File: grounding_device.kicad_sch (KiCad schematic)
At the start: 118 parts, among them IC1 NE555P, IC2 NE555P, IC3 NE555P, IC4 NE555P, Q1 2N2222, Q10 2N2222, Q11 2N2222, Q12 2N2222, Q2 2N2222, Q3 2N2222, Q4 2N2222, Q5 2N2222, Q6 2N2222, Q7 2N2222, Q8 2N2222, Q9 2N2222

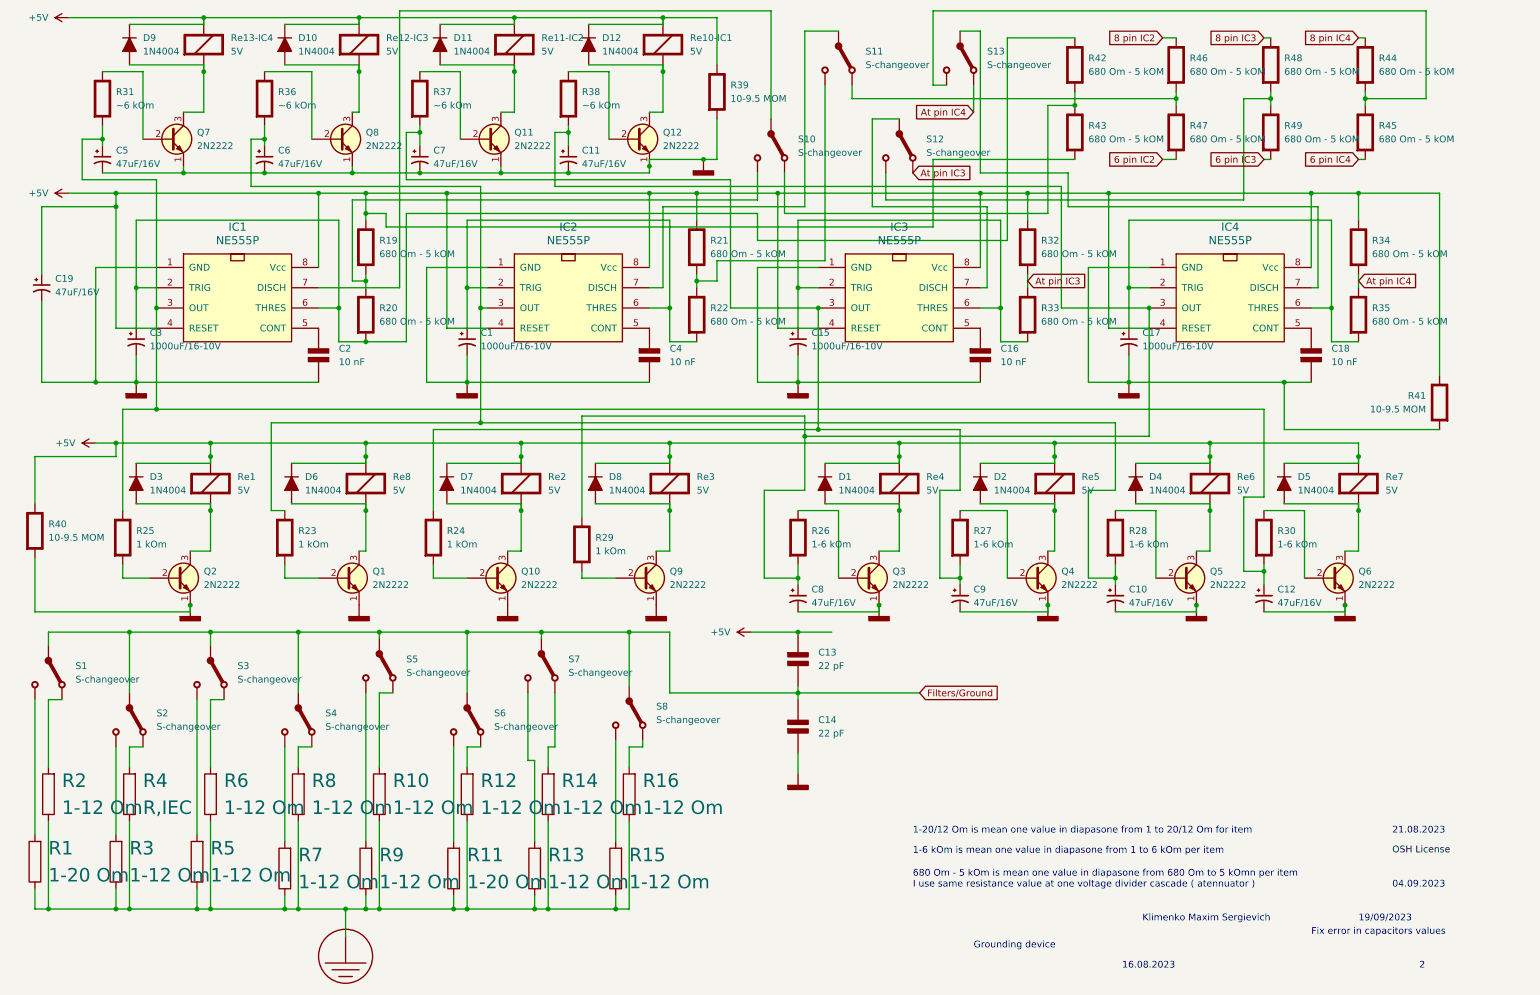
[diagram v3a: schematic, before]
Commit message: Upgrade to 4 revision
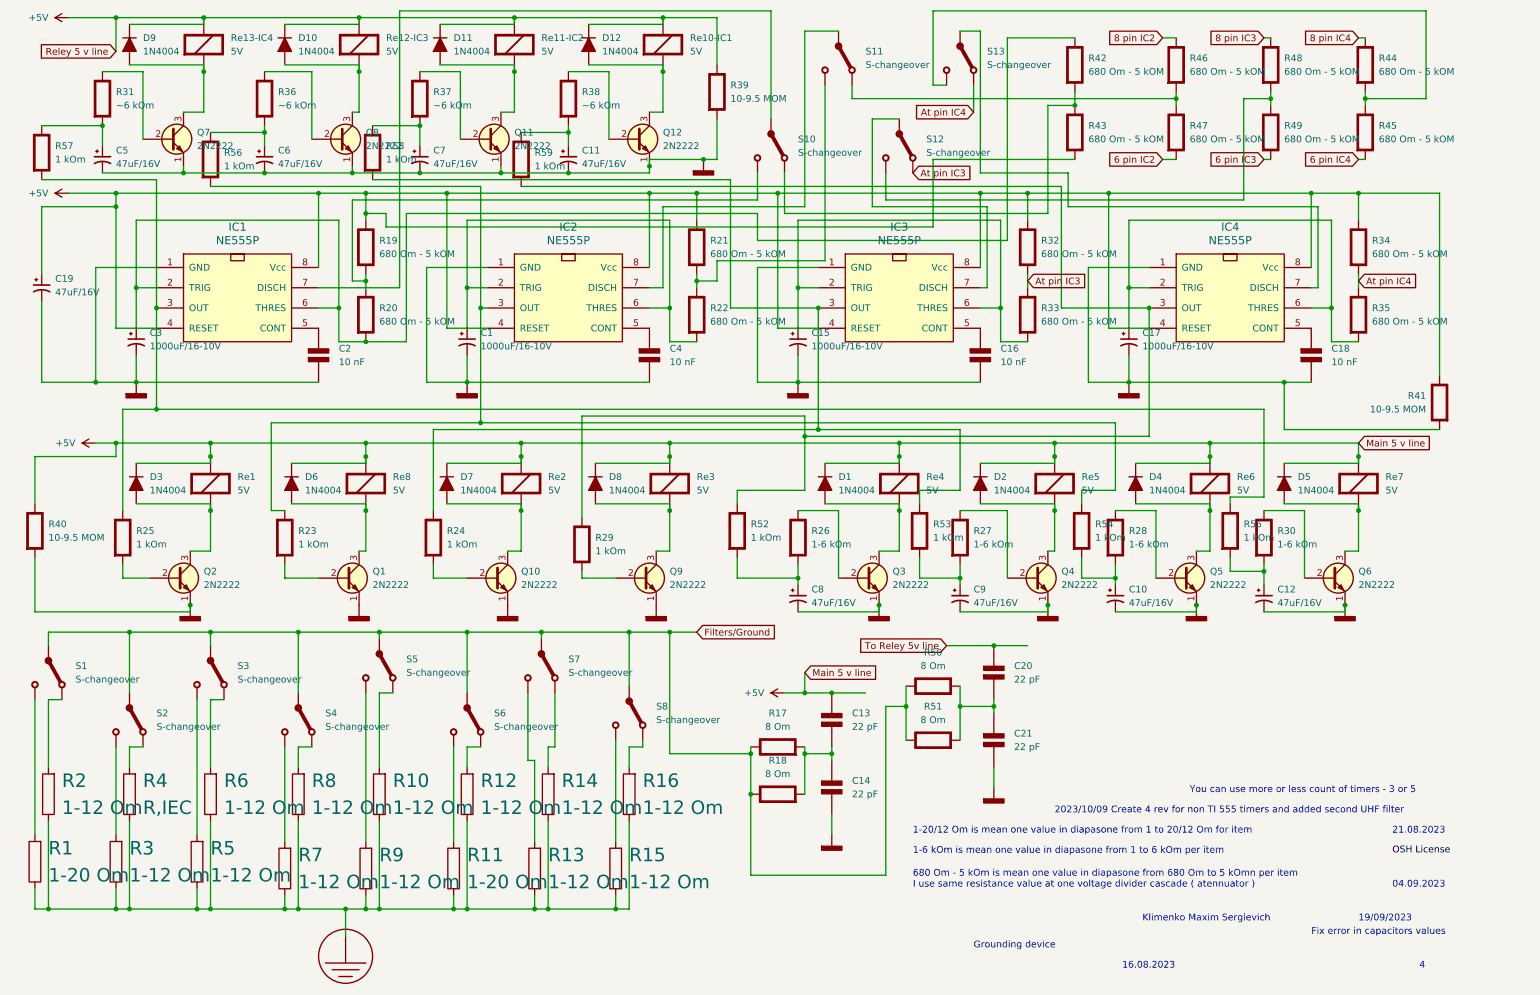
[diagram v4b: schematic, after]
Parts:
- added C20, C21: 22 pF, symbol PCM_Elektuur:C
- added R17, R18, R50, R51: 8 Om, symbol PCM_Elektuur:R
- added R52, R53, R54, R55, R56, R57, R58, R59: 1 kOm, symbol PCM_Elektuur:R
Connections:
- net 0: now also C21.2 (-)
- net Filters/Ground: now also R17.1 (+), R18.1 (+), R50.1 (+), R51.1 (+); no longer C13.2 (-), C14.1 (+)
- new net: C20.2 (-), C21.1 (+), R50.2 (-), R51.2 (-)
- new net: IC1.3 (OUT), R25.1 (+), R55.1 (+), R57.2 (-)
- new net: C5.1, R31.2 (-), R57.1 (+)
- new net: C12.1, R30.2 (-), R55.2 (-)
- new net: C11.1, R38.2 (-), R59.1 (+)
- new net: C7.1, R37.2 (-), R58.1 (+)
- new net: C9.1, R27.2 (-), R53.2 (-)
- new net: IC4.3 (OUT), R29.1 (+), R52.1 (+), R59.2 (-)
- new net: C8.1, R26.2 (-), R52.2 (-)
- new net: C13.2 (-), C14.1 (+), R17.2 (-), R18.2 (-)
- new net: IC3.3 (OUT), R24.1 (+), R53.1 (+), R58.2 (-)
- new net: C6.1, R36.2 (-), R56.1 (+)
- new net: IC2.3 (OUT), R23.1 (+), R54.1 (+), R56.2 (-)
- new net: C10.1, R28.2 (-), R54.2 (-)
- new net To Reley 5v line : C20.1 (+)
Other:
- note added: "2023/10/09 Create 4 rev for non TI 555 timers and added second UHF filter"
- note added: "4"
- note added: "You can use more or less count of timers - 3 or 5"
- note removed: "2"
- moved on the sheet: C13, C14

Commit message: Upgrade
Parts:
- added C22: 47uF or 100uF, symbol PCM_Elektuur:C
- added C23: 680pF, symbol PCM_Elektuur:C
- added R60, R61, R62, R63: 8 Om, symbol PCM_Elektuur:R
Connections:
- net Filters/Ground: now also R60.1 (+), R61.1 (+), R62.1 (+), R63.1 (+)
- net To Reley 5v line : now also C22.1 (+), C23.1 (+)
- new net: C22.2 (-), R60.2 (-), R61.2 (-)
- new net: C23.2 (-), R62.2 (-), R63.2 (-)
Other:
- note added: "Resistor array must be created for first"
- note added: "This 2 filters must be soldering after resistors array to (+)line before place rele"
- note added: "Updated 2023.10.23"

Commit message: Upgrade
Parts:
- removed R51, R60, R63: 8 Om, symbol PCM_Elektuur:R
- added C24: 47uF or 10uF, symbol PCM_Elektuur:C
- C22: value 47uF or 100uF -> 47uF or 10uF
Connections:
- net Filters/Ground: now also C24.1 (+); no longer R18.1 (+)
- net To Reley 5v line : now also R18.1 (+)
- net at C13.2 (-), C14.1 (+), R17.2 (-): no longer R18.2 (-)
- new net: C24.2 (-), R18.2 (-)
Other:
- note added: "04.03.2024"
- moved on the sheet: R17, R50, R61, R62

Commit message: Upgrade
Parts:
- C22, C24: value 47uF or 10uF -> 1uF
- C23: value 680pF -> 100pF
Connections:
- net 0: now also C24.1 (+)
- net Filters/Ground: now also R18.1 (+); no longer C24.1 (+)
- net To Reley 5v line : no longer R18.1 (+)
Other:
- moved on the sheet: C24, R18
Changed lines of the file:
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@@
 (kicad_sch (version 20230121) (generator eeschema)
   (paper "A4")
+  (junction (at 165.1 167.64) (diameter 0) (color 0 0 0 0)
+  )
   (junction (at 26.67 83.82) (diameter 0) (color 0 0 0 0)
   )
@@
   (junction (at 106.68 97.79) (diameter 0) (color 0 0 0 0)
   )
-  (junction (at 240.03 133.35) (diameter 0) (color 0 0 0 0)
-  )
   (junction (at 73.66 182.88) (diameter 0) (color 0 0 0 0)
   )
@@
   (junction (at 201.93 48.26) (diameter 0) (color 0 0 0 0)
   )
-  (junction (at 240.03 154.94) (diameter 0) (color 0 0 0 0)
-  )
   (junction (at 247.65 30.48) (diameter 0) (color 0 0 0 0)
   )
@@
   (junction (at 162.56 92.71) (diameter 0) (color 0 0 0 0)
   )
+  (junction (at 170.18 176.53) (diameter 0) (color 0 0 0 0)
+  )
   (junction (at 160.02 93.98) (diameter 0) (color 0 0 0 0)
   )
@@
     (stroke (width 0) (type default))
   )
+  (wire (pts (xy 156.21 187.96) (xy 170.18 187.96))
+    (stroke (width 0) (type default))
+  )
   (wire (pts (xy 48.26 182.88) (xy 62.23 182.88))
     (stroke (width 0) (type default))
@@
     (stroke (width 0) (type default))
   )
-  (wire (pts (xy 165.1 165.1) (xy 165.1 168.91))
+  (wire (pts (xy 165.1 165.1) (xy 165.1 167.64))
     (stroke (width 0) (type default))
   )
@@
     (stroke (width 0) (type default))
   )
-  (wire (pts (xy 224.79 69.85) (xy 208.28 69.85))
+  (wire (pts (xy 156.21 167.64) (xy 165.1 167.64))
     (stroke (width 0) (type default))
   )
-  (wire (pts (xy 173.99 115.57) (xy 177.8 115.57))
+  (wire (pts (xy 224.79 69.85) (xy 208.28 69.85))
     (stroke (width 0) (type default))
   )
-  (wire (pts (xy 256.54 154.94) (xy 251.46 154.94))
+  (wire (pts (xy 173.99 115.57) (xy 177.8 115.57))
     (stroke (width 0) (type default))
   )
@@
     (stroke (width 0) (type default))
   )
-  (wire (pts (xy 240.03 154.94) (xy 240.03 153.67))
+  (wire (pts (xy 240.03 153.67) (xy 240.03 157.48))
     (stroke (width 0) (type default))
   )
@@
     (stroke (width 0) (type default))
   )
-  (wire (pts (xy 240.03 157.48) (xy 240.03 154.94))
-    (stroke (width 0) (type default))
-  )
   (wire (pts (xy 213.36 160.02) (xy 199.39 160.02))
     (stroke (width 0) (type default))
@@
     (stroke (width 0) (type default))
   )
-  (wire (pts (xy 240.03 133.35) (xy 251.46 133.35))
-    (stroke (width 0) (type default))
-  )
   (wire (pts (xy 154.94 73.66) (xy 162.56 73.66))
     (stroke (width 0) (type default))
@@
     (stroke (width 0) (type default))
   )
-  (wire (pts (xy 248.92 134.62) (xy 248.92 154.94))
-    (stroke (width 0) (type default))
-  )
-  (wire (pts (xy 248.92 154.94) (xy 240.03 154.94))
-    (stroke (width 0) (type default))
-  )
   (wire (pts (xy 151.13 57.15) (xy 151.13 52.07))
     (stroke (width 0) (type default))
@@
     (stroke (width 0) (type default))
   )
-  (wire (pts (xy 256.54 134.62) (xy 248.92 134.62))
-    (stroke (width 0) (type default))
-  )
   (wire (pts (xy 99.06 69.85) (xy 99.06 46.99))
     (stroke (width 0) (type default))
@@
     (stroke (width 0) (type default))
   )
+  (wire (pts (xy 170.18 176.53) (xy 149.86 176.53))
+    (stroke (width 0) (type default))
+  )
   (wire (pts (xy 175.26 163.83) (xy 175.26 176.53))
     (stroke (width 0) (type default))
@@
     (stroke (width 0) (type default))
   )
-  (wire (pts (xy 251.46 154.94) (xy 251.46 133.35))
-    (stroke (width 0) (type default))
-  )
   (wire (pts (xy 74.93 49.53) (xy 74.93 64.77))
     (stroke (width 0) (type default))
@@
     (stroke (width 0) (type default))
   )
+  (wire (pts (xy 170.18 187.96) (xy 170.18 176.53))
+    (stroke (width 0) (type default))
+  )
   (wire (pts (xy 147.32 104.14) (xy 160.02 104.14))
     (stroke (width 0) (type default))
@@
     (stroke (width 0) (type default))
   )
+  (wire (pts (xy 165.1 167.64) (xy 165.1 168.91))
+    (stroke (width 0) (type default))
+  )
   (wire (pts (xy 130.81 48.26) (xy 139.7 48.26))
     (stroke (width 0) (type default))
@@
     (stroke (width 0) (type default))
   )
-  (wire (pts (xy 175.26 176.53) (xy 149.86 176.53))
+  (wire (pts (xy 175.26 176.53) (xy 170.18 176.53))
     (stroke (width 0) (type default))
   )
@@
     )
   )
-  (symbol (lib_id "PCM_Elektuur:C") (at 256.54 139.7 0) (unit 1)
+  (symbol (lib_id "PCM_Elektuur:C") (at 156.21 172.72 0) (unit 1)
     (in_bom yes) (on_board yes) (dnp no) (fields_autoplaced)
-    (property "Reference" "C24" (at 260.35 138.43 0)
+    (property "Reference" "C24" (at 160.02 171.45 0)
       (effects (font (size 1.27 1.27)) (justify left))
     )
-    (property "Value" "47uF or 10uF" (at 260.35 140.97 0)
+    (property "Value" "1uF" (at 160.02 173.99 0)
       (effects (font (size 1.27 1.27)) (justify left))
     )
-    (property "Footprint" "" (at 256.54 139.7 0)
+    (property "Footprint" "" (at 156.21 172.72 0)
       (effects (font (size 1.27 1.27)) hide)
     )
-    (property "Datasheet" "" (at 256.54 139.7 0)
+    (property "Datasheet" "" (at 156.21 172.72 0)
       (effects (font (size 1.27 1.27)) hide)
     )
-    (property "Indicator" "+" (at 255.27 136.525 0)
+    (property "Indicator" "+" (at 154.94 169.545 0)
       (effects (font (size 1.27 1.27)) hide)
     )
-    (property "Rating" "V" (at 255.905 142.875 0)
+    (property "Rating" "V" (at 155.575 175.895 0)
       (effects (font (size 1.27 1.27)) (justify right) hide)
     )
@@
       (effects (font (size 1.27 1.27)) (justify left))
     )
-    (property "Value" "47uF or 10uF" (at 217.17 139.7 0)
+    (property "Value" "1uF" (at 217.17 139.7 0)
       (effects (font (size 1.27 1.27)) (justify left))
     )
@@
     )
   )
-  (symbol (lib_id "PCM_Elektuur:R") (at 256.54 149.86 180) (unit 1)
+  (symbol (lib_id "PCM_Elektuur:R") (at 156.21 182.88 180) (unit 1)
     (in_bom yes) (on_board yes) (dnp no) (fields_autoplaced)
-    (property "Reference" "R18" (at 259.715 148.59 0)
+    (property "Reference" "R18" (at 159.385 181.61 0)
       (effects (font (size 1.27 1.27)) (justify right))
     )
-    (property "Value" "8 Om" (at 259.715 151.13 0)
+    (property "Value" "8 Om" (at 159.385 184.15 0)
       (effects (font (size 1.27 1.27)) (justify right))
     )
-    (property "Footprint" "" (at 256.54 149.86 0)
+    (property "Footprint" "" (at 156.21 182.88 0)
       (effects (font (size 1.27 1.27)) hide)
     )
-    (property "Datasheet" "" (at 256.54 149.86 0)
+    (property "Datasheet" "" (at 156.21 182.88 0)
       (effects (font (size 1.27 1.27)) hide)
     )
-    (property "Indicator" "+" (at 259.715 153.035 0)
+    (property "Indicator" "+" (at 159.385 186.055 0)
       (effects (font (size 1.27 1.27)) hide)
     )
-    (property "Rating" "W" (at 254 146.685 0)
+    (property "Rating" "W" (at 153.67 179.705 0)
       (effects (font (size 1.27 1.27)) (justify left) hide)
     )
@@
       (effects (font (size 1.27 1.27)) (justify left))
     )
-    (property "Value" "680pF" (at 243.84 139.7 0)
+    (property "Value" "100pF" (at 243.84 139.7 0)
       (effects (font (size 1.27 1.27)) (justify left))
     )

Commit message: Upgrade
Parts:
- added C25: 100pF, symbol PCM_Elektuur:C
- added C26, C27: 10pF, symbol PCM_Elektuur:C
- added R51: 2 Om, symbol PCM_Elektuur:R
- C22, C24: value 1uF -> 10uF
- R17, R50: value 8 Om -> 1 Om
- R18, R61: value 8 Om -> 2Om
- R62: value 8 Om -> 2 Om
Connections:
- net 0: now also C25.2 (-), C27.2 (-)
- net Filters/Ground: now also R51.1 (+)
- net To Reley 5v line : now also C26.1 (+)
- net at C23.2 (-), R62.2 (-): now also C25.1 (+)
- new net: C26.2 (-), C27.1 (+), R51.2 (-)
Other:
- moved on the sheet: R62
